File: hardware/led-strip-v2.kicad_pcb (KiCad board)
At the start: 2 copper layers, 30 x 30 mm, 42 parts, among them J1 AKL_5_2, J2 AKL_5_2, J3 AKL_5_2, P1 CON-SENSOR, P2 TST, P3 TST, P4 TST, P5 TST, P6 TST, P7 TST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

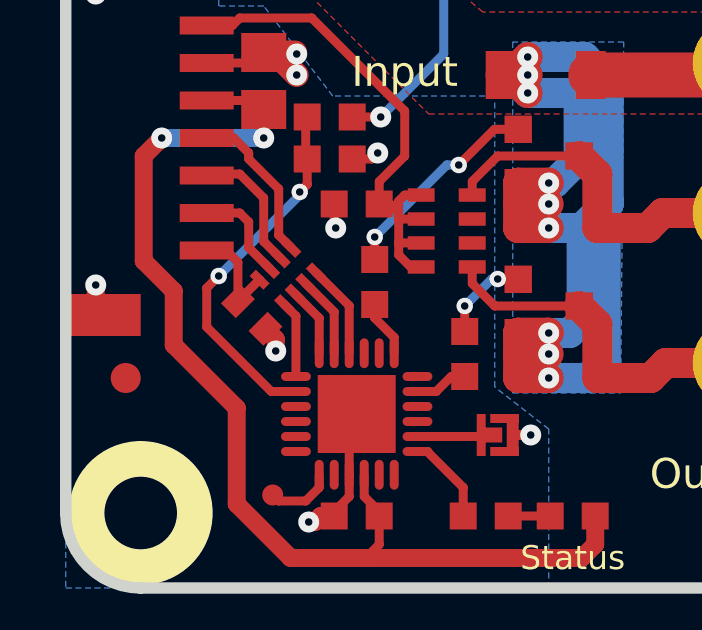
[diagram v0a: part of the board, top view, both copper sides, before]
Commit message: Change capacitor footprint(s) to C0402F
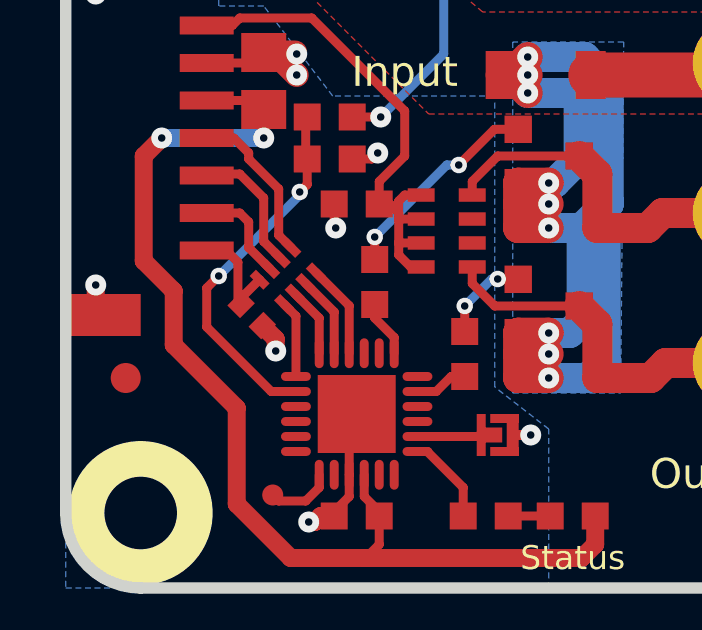
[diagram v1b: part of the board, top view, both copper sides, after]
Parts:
- C1: footprint C0402E -> kicad-libraries:C0402F
- D3: footprint D0603F -> kicad-libraries:D0603F
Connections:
- RP3 pad 2: (no net) -> Net-(RP3-Pad2)
- RP3 pad 3: (no net) -> Net-(RP3-Pad3)
- U1 pad 11: (no net) -> Net-(U1-Pad11)
- U1 pad 12: (no net) -> Net-(U1-Pad12)
- U1 pad 15: (no net) -> Net-(U1-Pad15)
- U1 pad 16: (no net) -> Net-(U1-Pad16)
- U1 pad 18: (no net) -> Net-(U1-Pad18)
- U1 pad 20: (no net) -> Net-(U1-Pad20)
- U1 pad 21: (no net) -> Net-(U1-Pad21)
- U1 pad 3: (no net) -> Net-(U1-Pad3)
- U1 pad 4: (no net) -> Net-(U1-Pad4)
- U1 pad 5: (no net) -> Net-(U1-Pad5)
- U1 pad 6: (no net) -> Net-(U1-Pad6)
- U1 pad 8: (no net) -> Net-(U1-Pad8)
